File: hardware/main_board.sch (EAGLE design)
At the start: 113 parts, among them IC1 IC_USBLC6-2, IC2 LM1117IMPX-3.3, IC3 PIC32MX795F512, IC4 ENC28J60, IC5 LM1117MPX-2.5, U1 USD-SOCKETUSD, U2 VS1003, X2 CRYSTALS-NOGND-CFPX-217, X3 KUSBVX, Y1 CRYSTAL-GROUNDEDSMD-5X3.2, Y2 CRYSTAL-GROUNDEDSMD-5X3.2, Y3 CRYSTAL-GROUNDEDSMD-5X3.2

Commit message: PCB updated
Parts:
- removed R14: (no value), rcl:R-EU_R1206
- C38: device rcl:C-EUC0603 -> rcl:C-EUC0402
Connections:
- net RG7 renamed RG7_SDA2A
- net RG8 renamed RG8_SCL2A
- removed net 3V_IN: C14.1, C15.+, C18.1, C19.1, C25.1, C26.+, C29.1, C31.1, C32.1, C40.1, C41.1, C42.1, C56.1, IC2.OUT, IC2.OUT1, IC4.VDD, IC4.VDDOSC, IC4.VDDPLL, IC4.VDDRX, IC4.VDDTX, JP3.4, L3.1, R11.2, R13.2, R14.1, R30.2, R8.2, SV1.33, SV1.34, U$2.!HOLD, U$2.!WP, U$2.VDD, U1.VCC, U2G$1.TEST, U2P.IOVDD, U2P.IOVDD1, U2P.IOVDD2
- net 3V: now also C14.1, C15.+, C18.1, C19.1, C25.1, C26.+, C29.1, C31.1, C32.1, C40.1, C41.1, C42.1, C56.1, IC2.OUT, IC2.OUT1, IC4.VDD, IC4.VDDOSC, IC4.VDDPLL, IC4.VDDRX, IC4.VDDTX, JP3.4, L3.1, R11.2, R13.2, R30.2, R8.2, SV1.33, SV1.34, U$2.!HOLD, U$2.!WP, U$2.VDD, U1.VCC, U2G$1.TEST, U2P.IOVDD, U2P.IOVDD1, U2P.IOVDD2; no longer R14.2

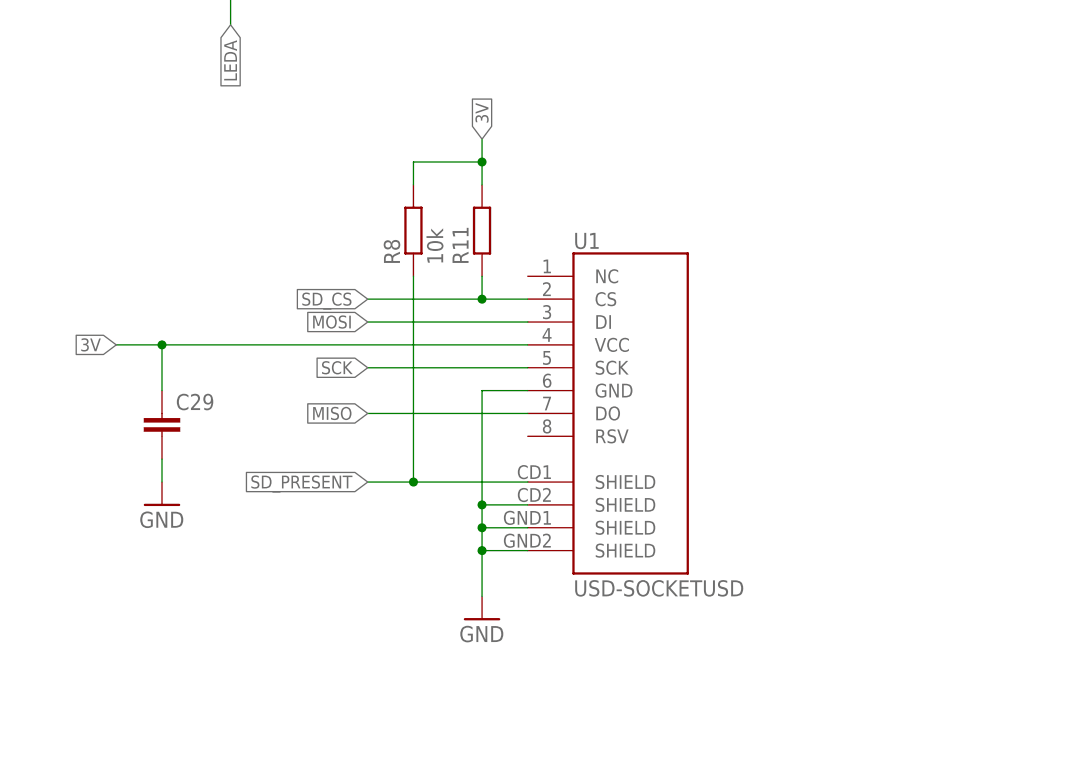
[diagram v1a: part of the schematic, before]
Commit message: MISO pull-up added
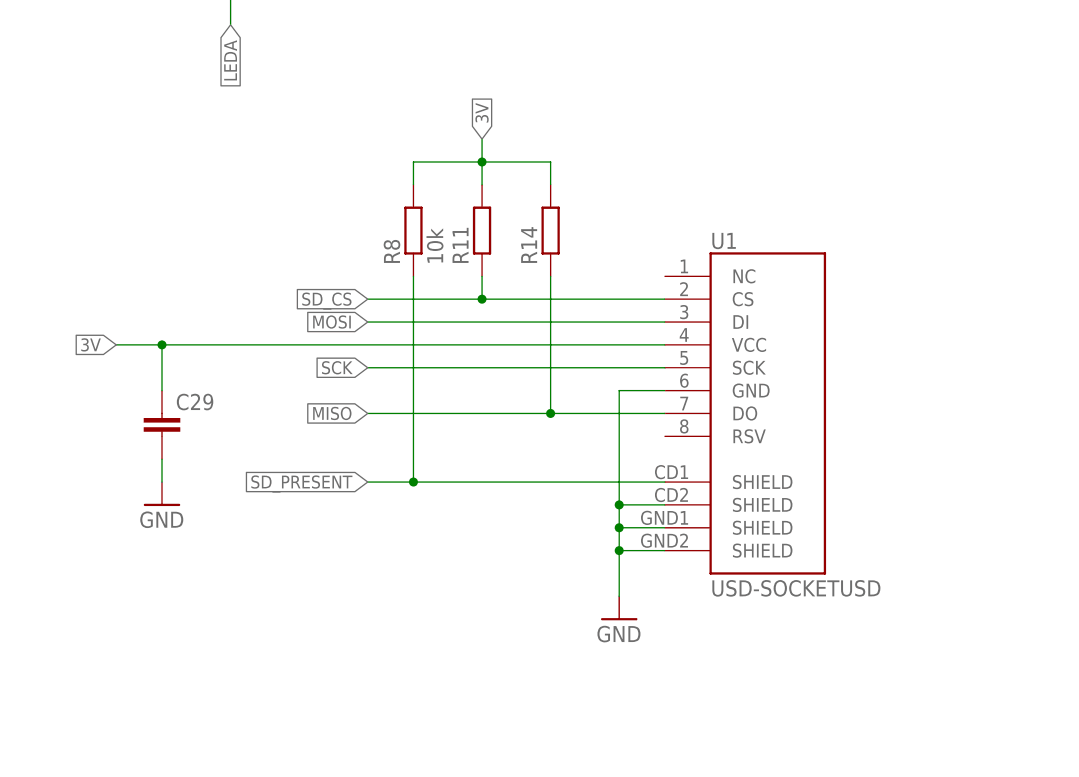
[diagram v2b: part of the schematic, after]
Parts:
- added R14: (no value), rcl:R-EU_R0603
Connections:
- net 3V: now also R14.2
- net MISO: now also R14.1
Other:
- moved on the sheet: U1
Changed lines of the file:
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@@
 <?xml version="1.0" encoding="utf-8"?>
 <!DOCTYPE eagle SYSTEM "eagle.dtd">
-<eagle version="7.2.0">
+<eagle version="7.7.0">
 <drawing>
 <settings>
@@
 <part name="GND53" library="supply1" deviceset="GND" device=""/>
 <part name="SV1" library="con-harting-ml" deviceset="ML34" device="L"/>
+<part name="R14" library="rcl" deviceset="R-EU_" device="R0603"/>
 </parts>
 <sheets>
@@
 <instance part="R12" gate="G$1" x="73.66" y="83.82"/>
 <instance part="Y2" gate="G$1" x="73.66" y="157.48" rot="R90"/>
-<instance part="U1" gate="G$1" x="254" y="81.28"/>
-<instance part="GND47" gate="1" x="241.3" y="55.88"/>
+<instance part="U1" gate="G$1" x="269.24" y="81.28"/>
+<instance part="GND47" gate="1" x="256.54" y="55.88"/>
 <instance part="R11" gate="G$1" x="241.3" y="99.06" rot="R90"/>
 <instance part="C29" gate="G$1" x="205.74" y="78.74"/>
@@
 <instance part="GND53" gate="1" x="510.54" y="198.12" rot="R180"/>
 <instance part="SV1" gate="G$1" x="332.74" y="264.16"/>
+<instance part="R14" gate="G$1" x="248.92" y="99.06" rot="R90"/>
 </instances>
 <busses>
@@
 <pinref part="GND47" gate="1" pin="GND"/>
 <pinref part="U1" gate="G$1" pin="SHIELD@4"/>
-<wire x1="241.3" y1="66.04" x2="241.3" y2="63.5" width="0.1524" layer="91"/>
-<wire x1="241.3" y1="63.5" x2="241.3" y2="58.42" width="0.1524" layer="91"/>
-<wire x1="246.38" y1="63.5" x2="241.3" y2="63.5" width="0.1524" layer="91"/>
-<junction x="241.3" y="63.5"/>
+<wire x1="256.54" y1="66.04" x2="256.54" y2="63.5" width="0.1524" layer="91"/>
+<wire x1="256.54" y1="63.5" x2="256.54" y2="58.42" width="0.1524" layer="91"/>
+<wire x1="261.62" y1="63.5" x2="256.54" y2="63.5" width="0.1524" layer="91"/>
+<junction x="256.54" y="63.5"/>
 <pinref part="U1" gate="G$1" pin="SHIELD@3"/>
-<wire x1="246.38" y1="66.04" x2="241.3" y2="66.04" width="0.1524" layer="91"/>
-<junction x="241.3" y="66.04"/>
+<wire x1="261.62" y1="66.04" x2="256.54" y2="66.04" width="0.1524" layer="91"/>
+<junction x="256.54" y="66.04"/>
 <pinref part="U1" gate="G$1" pin="GND"/>
-<wire x1="246.38" y1="81.28" x2="241.3" y2="81.28" width="0.1524" layer="91"/>
-<wire x1="241.3" y1="81.28" x2="241.3" y2="68.58" width="0.1524" layer="91"/>
+<wire x1="261.62" y1="81.28" x2="256.54" y2="81.28" width="0.1524" layer="91"/>
+<wire x1="256.54" y1="81.28" x2="256.54" y2="68.58" width="0.1524" layer="91"/>
 <pinref part="U1" gate="G$1" pin="SHIELD@2"/>
-<wire x1="241.3" y1="68.58" x2="241.3" y2="66.04" width="0.1524" layer="91"/>
-<wire x1="246.38" y1="68.58" x2="241.3" y2="68.58" width="0.1524" layer="91"/>
-<junction x="241.3" y="68.58"/>
+<wire x1="256.54" y1="68.58" x2="256.54" y2="66.04" width="0.1524" layer="91"/>
+<wire x1="261.62" y1="68.58" x2="256.54" y2="68.58" width="0.1524" layer="91"/>
+<junction x="256.54" y="68.58"/>
 </segment>
 <segment>
@@
 <segment>
 <pinref part="U1" gate="G$1" pin="VCC"/>
-<wire x1="246.38" y1="86.36" x2="205.74" y2="86.36" width="0.1524" layer="91"/>
+<wire x1="261.62" y1="86.36" x2="205.74" y2="86.36" width="0.1524" layer="91"/>
 <pinref part="C29" gate="G$1" pin="1"/>
 <wire x1="205.74" y1="86.36" x2="200.66" y2="86.36" width="0.1524" layer="91"/>
@@
 <pinref part="R8" gate="G$1" pin="2"/>
 <wire x1="233.68" y1="106.68" x2="233.68" y2="104.14" width="0.1524" layer="91"/>
+<pinref part="R14" gate="G$1" pin="2"/>
+<wire x1="241.3" y1="106.68" x2="248.92" y2="106.68" width="0.1524" layer="91"/>
+<wire x1="248.92" y1="106.68" x2="248.92" y2="104.14" width="0.1524" layer="91"/>
 </segment>
 <segment>
@@
 <segment>
 <pinref part="U1" gate="G$1" pin="SCK"/>
-<wire x1="246.38" y1="83.82" x2="228.6" y2="83.82" width="0.1524" layer="91"/>
+<wire x1="261.62" y1="83.82" x2="228.6" y2="83.82" width="0.1524" layer="91"/>
 <label x="228.6" y="83.82" size="1.4224" layer="95" rot="R180" xref="yes"/>
 </segment>
@@
 <segment>
 <pinref part="U1" gate="G$1" pin="DO"/>
-<wire x1="246.38" y1="78.74" x2="228.6" y2="78.74" width="0.1524" layer="91"/>
+<wire x1="261.62" y1="78.74" x2="248.92" y2="78.74" width="0.1524" layer="91"/>
 <label x="228.6" y="78.74" size="1.4224" layer="95" rot="R180" xref="yes"/>
+<pinref part="R14" gate="G$1" pin="1"/>
+<wire x1="248.92" y1="78.74" x2="228.6" y2="78.74" width="0.1524" layer="91"/>
+<wire x1="248.92" y1="93.98" x2="248.92" y2="78.74" width="0.1524" layer="91"/>
+<junction x="248.92" y="78.74"/>
 </segment>
 <segment>
@@
 <segment>
 <pinref part="U1" gate="G$1" pin="DI"/>
-<wire x1="246.38" y1="88.9" x2="228.6" y2="88.9" width="0.1524" layer="91"/>
+<wire x1="261.62" y1="88.9" x2="228.6" y2="88.9" width="0.1524" layer="91"/>
 <label x="228.6" y="88.9" size="1.4224" layer="95" rot="R180" xref="yes"/>
 </segment>
@@
 <segment>
 <pinref part="U1" gate="G$1" pin="CS"/>
-<wire x1="246.38" y1="91.44" x2="241.3" y2="91.44" width="0.1524" layer="91"/>
+<wire x1="261.62" y1="91.44" x2="241.3" y2="91.44" width="0.1524" layer="91"/>
 <pinref part="R11" gate="G$1" pin="1"/>
 <wire x1="241.3" y1="91.44" x2="228.6" y2="91.44" width="0.1524" layer="91"/>
@@
 <segment>
 <pinref part="U1" gate="G$1" pin="SHIELD@1"/>
-<wire x1="246.38" y1="71.12" x2="233.68" y2="71.12" width="0.1524" layer="91"/>
+<wire x1="261.62" y1="71.12" x2="233.68" y2="71.12" width="0.1524" layer="91"/>
 <label x="228.6" y="71.12" size="1.4224" layer="95" rot="R180" xref="yes"/>
 <pinref part="R8" gate="G$1" pin="1"/>
